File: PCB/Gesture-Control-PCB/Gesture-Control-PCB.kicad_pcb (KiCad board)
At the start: 2 copper layers, 73 x 60 mm, 5 parts, among them J1 Jack-DC, J2 Conn_01x07_Female, U1 L7806CV, U2 LD1117V33, U3 NodeMCU1.0(ESP-12E)

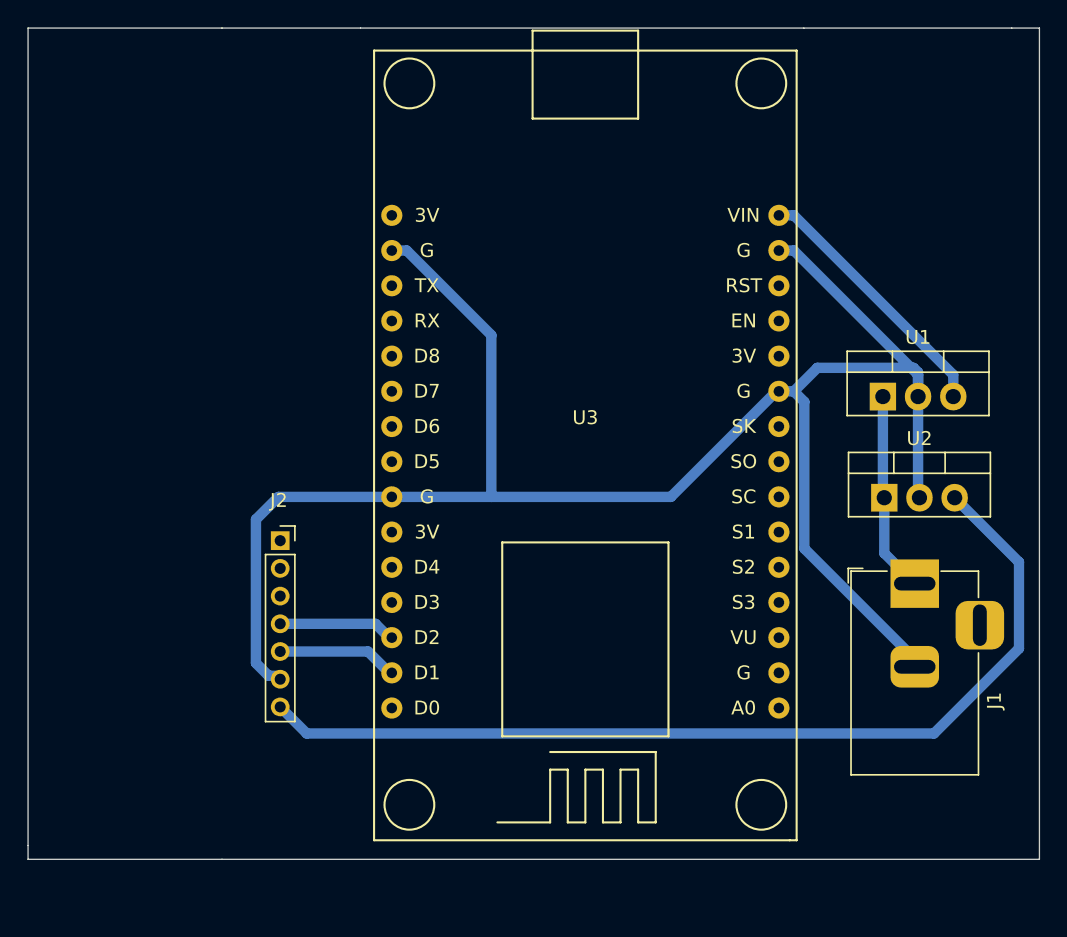
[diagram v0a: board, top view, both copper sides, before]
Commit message: decrease size, fit all components under nodemcu
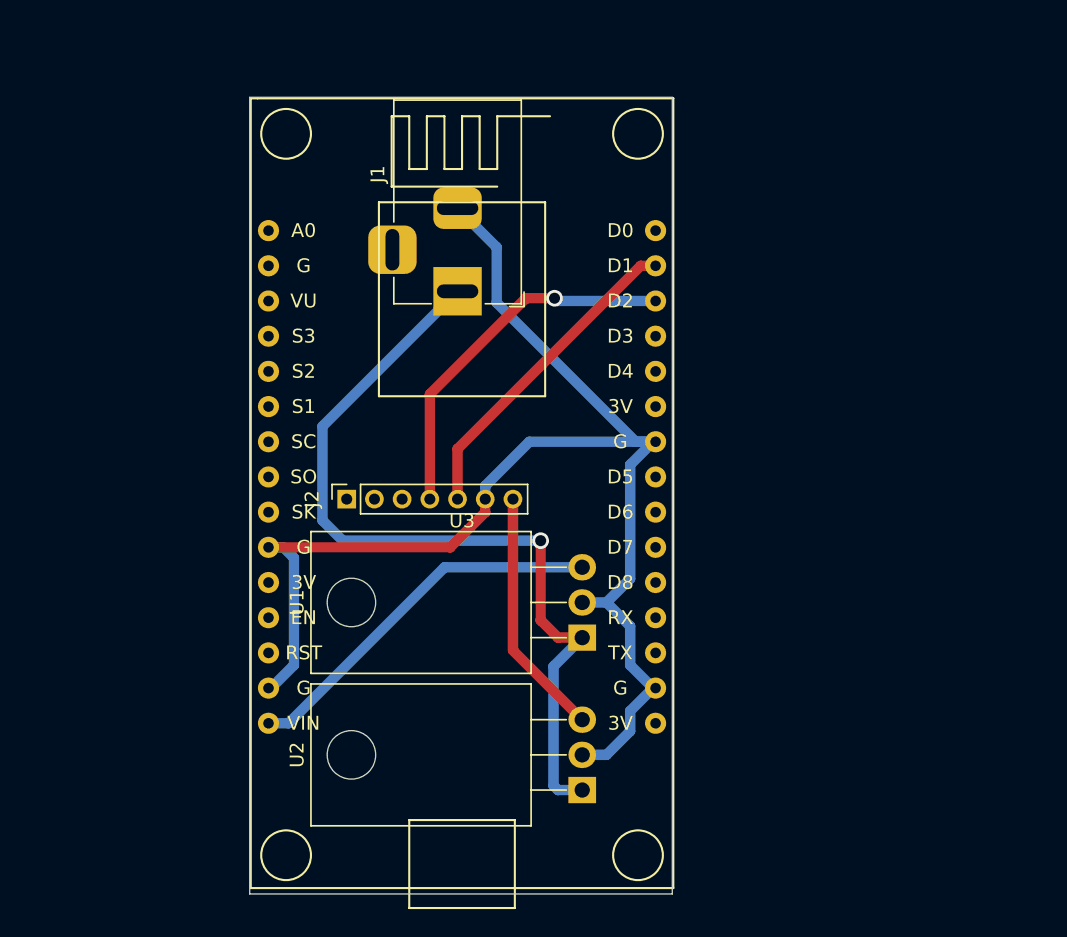
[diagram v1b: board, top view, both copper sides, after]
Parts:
- U1, U2: footprint Package_TO_SOT_THT:TO-220-3_Vertical -> Package_TO_SOT_THT:TO-220-3_Horizontal_TabDown
- moved J1 39.2 mm to (101.0, 82.0), turned to 270 degrees
- moved U2 30.3 mm to (110.0, 118.0), turned to 90 degrees
- moved U1 27.8 mm to (110.0, 107.0), turned to 90 degrees
- moved U3 11.6 mm to (101.3, 98.6), turned to 0 degrees
- moved J2 5.66 mm to (93.0, 97.0), turned to 90 degrees
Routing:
- net +3V3: track 69.5 -> 18.0 mm
- net +12V: track 14.5 -> 60.7 mm, vias 0 -> 1
- net GND: track 135.3 -> 98.9 mm
- net /SDA: track 8.47 -> 26.8 mm, vias 0 -> 1
- net /SCL: track 8.69 -> 23.4 mm
- net +6V: track 18.9 -> 27.3 mm
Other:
- board size 73 x 60 mm -> 30.5 x 57.5 mm
- net class Default: via_dia 0.8 -> 1.2; via_drill 0.4 -> 0.8
